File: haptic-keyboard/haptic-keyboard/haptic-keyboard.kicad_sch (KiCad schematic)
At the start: 0 parts

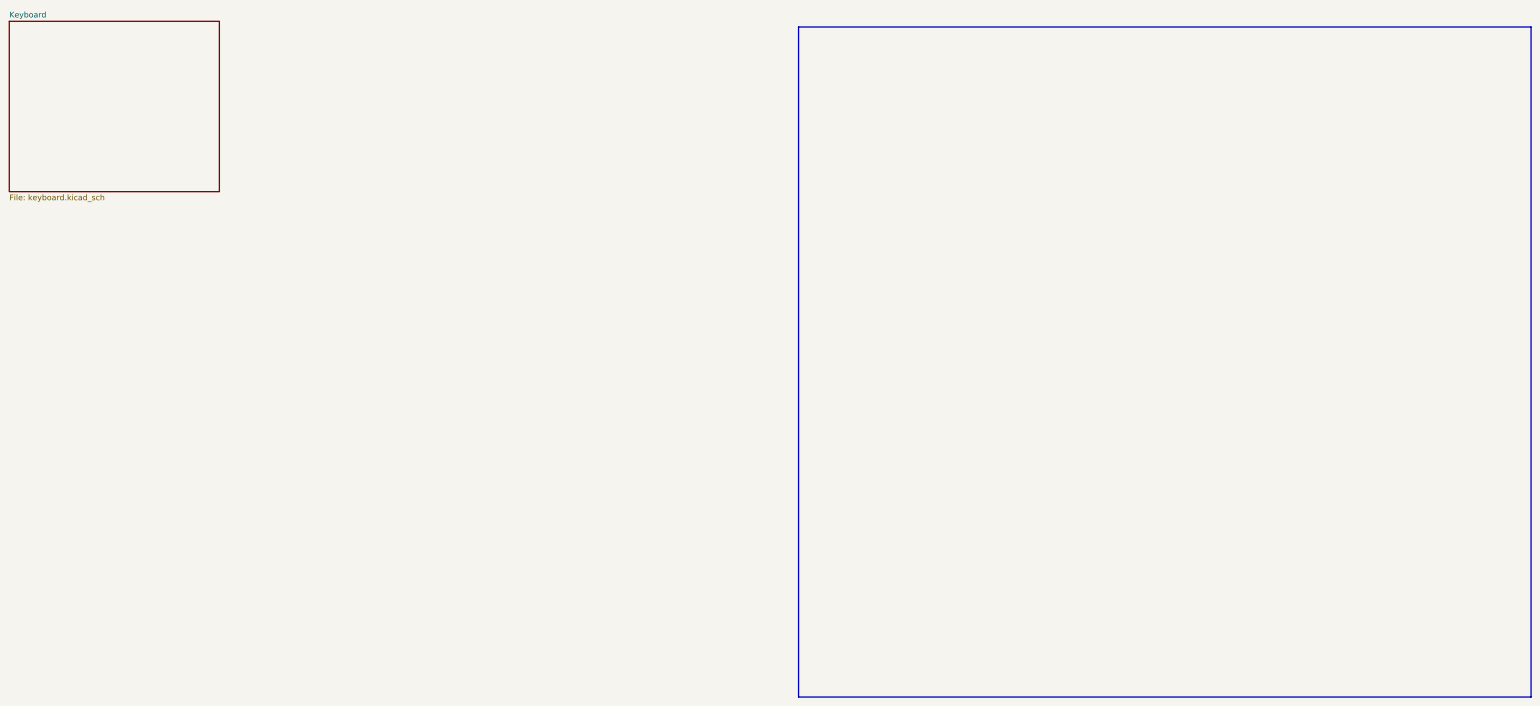
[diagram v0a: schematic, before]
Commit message: Added the initial schematic for it.
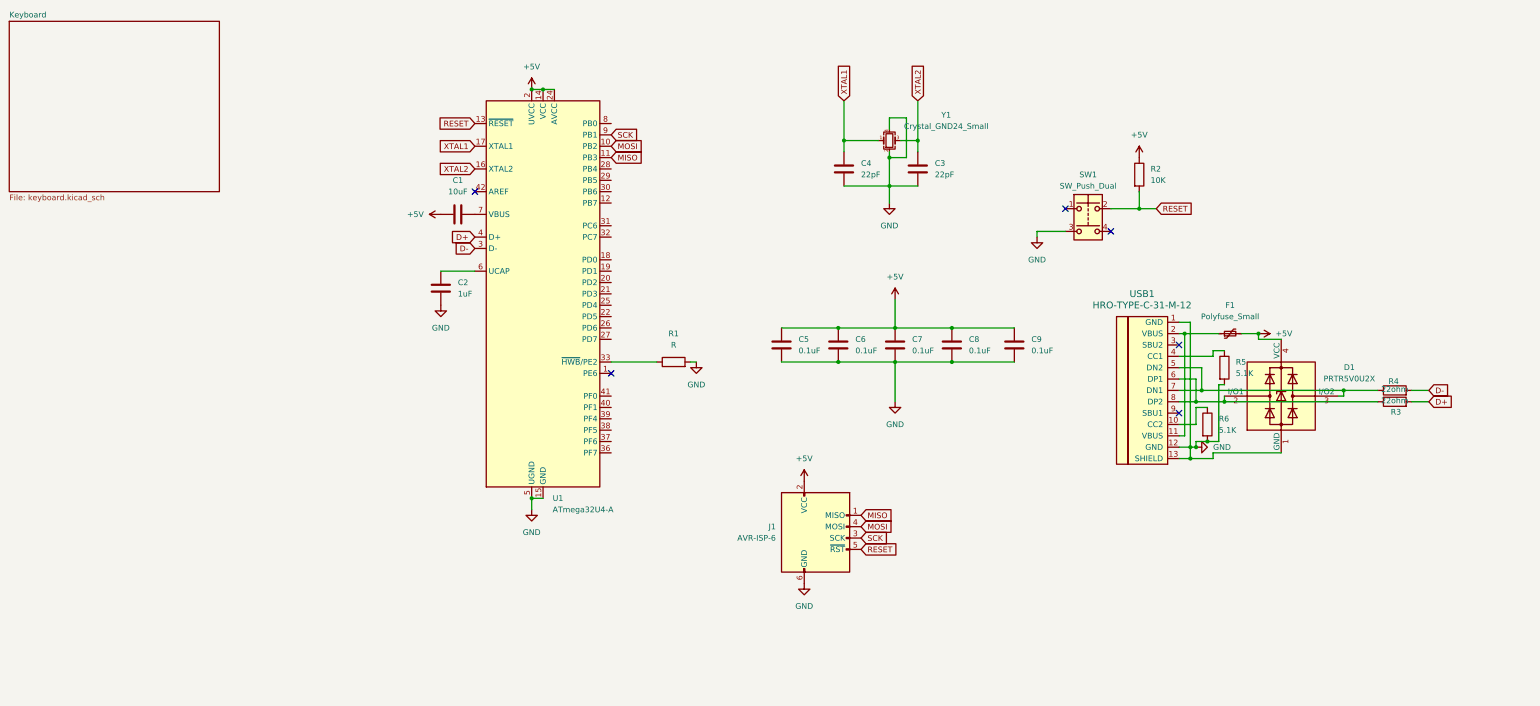
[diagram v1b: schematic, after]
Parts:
- added C1: 10uF, symbol Device:C
- added C2: 1uF, symbol Device:C
- added C3, C4: 22pF, symbol Device:C
- added C5, C6, C7, C8, C9: 0.1uF, symbol Device:C
- added D1: PRTR5V0U2X, Package_TO_SOT_SMD:SOT-143, symbol Power_Protection:PRTR5V0U2X
- added F1: Polyfuse_Small, symbol Device:Polyfuse_Small
- added J1: AVR-ISP-6, symbol Connector:AVR-ISP-6
- added R1: R, symbol Device:R
- added R2: 10K, symbol Device:R
- added R3, R4: 22ohm, symbol Device:R
- added R5, R6: 5.1K, symbol Device:R
- added SW1: SW_Push_Dual, symbol Switch:SW_Push_Dual
- added U1: ATmega32U4-A, Package_QFP:TQFP-44_10x10mm_P0.8mm, symbol MCU_Microchip_ATmega:ATmega32U4-A
- added USB1: HRO-TYPE-C-31-M-12, symbol USB-C:HRO-TYPE-C-31-M-12
- added Y1: Crystal_GND24_Small, symbol Device:Crystal_GND24_Small
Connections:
- new net: R6.1, USB1.10 (CC2)
- new net: R5.1, USB1.4 (CC1)
- new net: D1.3 (I/O2), R4.1, USB1.5 (DN2), USB1.7 (DN1)
- new net: C1.2, U1.7 (VBUS)
- new net: F1.1, USB1.11 (VBUS), USB1.2 (VBUS)
- new net: R1.1, U1.33 (~{HWB}/PE2)
- new net: D1.2 (I/O1), R3.1, USB1.6 (DP1), USB1.8 (DP2)
- new net: C2.1, U1.6 (UCAP)
- new net +5V: C1.1, C5.1, C6.1, C7.1, C8.1, C9.1, D1.4 (VCC), F1.2, J1.2 (VCC), R2.1, U1.14 (VCC), U1.2 (UVCC), U1.24 (AVCC), U1.34 (VCC), U1.44 (AVCC)
- new net D+: R3.2, U1.4 (D+)
- new net D-: R4.2, U1.3 (D-)
- new net GND: C2.2, C3.2, C4.1, C5.2, C6.2, C7.2, C8.2, C9.2, D1.1 (GND), J1.6 (GND), R1.2, R5.2, R6.2, SW1.3, U1.15 (GND), U1.23 (GND), U1.35 (GND), U1.43 (GND), U1.5 (UGND), USB1.1 (GND), USB1.12 (GND), USB1.13 (SHIELD), Y1.2, Y1.4
- new net MISO: J1.1 (MISO), U1.11 (PB3)
- new net MOSI: J1.4 (MOSI), U1.10 (PB2)
- new net RESET: J1.5 (~{RST}), R2.2, SW1.2, U1.13 (~{RESET})
- new net SCK: J1.3 (SCK), U1.9 (PB1)
- new net XTAL1: C4.2, U1.17 (XTAL1), Y1.1
- new net XTAL2: C3.1, U1.16 (XTAL2), Y1.3
- no-connect marks 0 -> 6
